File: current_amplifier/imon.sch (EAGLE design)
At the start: 32 parts, among them U1 AD8210, U2 AD1583_AD1583BRTZ-REEL7CT-ND, U3 FR014H5JZ, U4 OP-AMP_BALANCED, U6 LTC2312-12

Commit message: The imon current monitor board schematic is filled out
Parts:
- removed C1, C16: (no value), rcl_custom:C-EU0805-B
- removed R2: (no value), rcl_custom:R-US_0805-B
- removed U1: AD8210, marionette:AD8210
- removed U3: FR014H5JZ, marionette:FR014H5JZ
- added C105, C19: 1u, rcl_custom:C-EU0402-B
- added C18: np, rcl_custom:C-EU0402-B
- added C20: 6.2n, rcl_custom:C-EU0402-B
- added C50: 220p, rcl_custom:C-EU0402-B
- added C80: 100n, rcl_custom:C-EU0402-B
- added D1, D2: ESD8006-ESD8006, marionette:ESD8006-ESD8006
- added J1, R11, R16, R17: (no value), marionette:JUMPER-SHORTED-CUTTABLE-E0402-0.3MM
- added R10: 56, rcl_custom:R-US_0402-B
- added R12, R13, R19: np, rcl_custom:R-US_0402-B
- added R18: 1k, rcl_custom:R-US_0402-B
- added R30: 51, rcl_custom:R-US_0402-B
- added R40: 560, rcl_custom:R-US_0402-B
- added R67, R9: np, rcl_custom:R-US_1206-0402
- added TP1, TP10, TP11, TP9: PAD+VIA_0.25MM, marionette:PAD+VIA_0.25MM
- added TP2: PAD+VIA_0.6MM, marionette:PAD+VIA_0.6MM
- added TP3, TP4, TP5, TP6, TP7, TP8: (no value), marionette:PAD+X-1.0-NO_CREAM+SILK
- added U$1: MCP1501", marionette:MCP1501"
- C10, C3: value (none) -> 100n; device rcl_custom:C-EU0805-B -> rcl_custom:C-EU0402-B
- C11, C12, C13, C14, C15, C4: value (none) -> 1u; device rcl_custom:C-EU0805-B -> rcl_custom:C-EU0402-B
- C2: value (none) -> 2.7n; device rcl_custom:C-EU0805-B -> rcl_custom:C-EU0402-B
- C5: value (none) -> 220p; device rcl_custom:C-EU0805-B -> rcl_custom:C-EU0402-B
- C6, C7: value (none) -> 1u; device rcl_custom:C-EU0805-A-NOSILK -> rcl_custom:C-EU0402-B
- C9: value (none) -> np
- R1: value (none) -> 97.6; device rcl_custom:R-US_0805-B -> rcl_custom:R-US_0402-B
- R3: value (none) -> 88.7; device rcl_custom:R-US_0805-B -> rcl_custom:R-US_0402-B
- R4: value (none) -> 976; device rcl_custom:R-US_0805-B -> rcl_custom:R-US_0402-B
- R5, R6: device rcl_custom:R-US_0805-B -> rcl_custom:R-US_0402-B
- R7, R8: device rcl_custom:R-US_0805-B -> rcl_custom:R-US_1206-0402
- U2: value AD1583_AD1583BRTZ-REEL7CT-ND -> OPAMP_DUALFAN4852; device marionette:VREF_BANDGAP_AD1583_AD1583BRTZ-REEL7CT-ND -> marionette:OPAMP_DUALFAN4852; CHIP ADP1583 -> (none); DPN (none) -> FAN4852IMU8XCT-ND; VREF 3.0V -> (none)
- U4: value OP-AMP_BALANCED -> AD8418; device marionette:OP-AMP_BALANCED -> marionette:AD8418; DPN (none) -> AD8418WBRZ-ND
- U6: DPN (none) -> LTC2312CTS8-12#TRMPBFCT-ND
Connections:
- removed net N$15: R7.1, U1.IN+
- removed net N$7: R6.1, U4G1.BAL2
- new net C80: C6.2, C80.2, U4G3.V-
- new net N$11: R8.1, U4G1.IN-
- new net N$16: R5.2, R6.1, U$1.SHDN_N
- new net N$17: C50.1, R30.1, U2G2.-IN
- new net N$18: C50.2, R16.2, R40.1, TP5.P, U2G2.OUT
- new net N$19: C18.2, R16.1, R17.2, U6.AIN
- new net N$20: D2G3.CATHODE, JP2.1, R11.2
- new net N$21: J1.1, R19.1, TP9.TP, U4G1.VREF2
- new net N$22: R12.1, TP1.TP
- new net VREF_FILTERED: C105.2, C7.2, J1.2, R12.2, R13.1, R18.2, TP10.TP, TP11.TP, U4G1.VREF1
- new net VREF_OUT: R18.1, U$1.VOUT
- net GND: now also C105.1, C14.1, C15.1, C18.1, C19.2, C2.1, C20.1, C7.1, D1G7.PIN, D2G7.PIN, R13.2, R19.2, R5.1, U$1.GND, U2G1.+IN, U2G2.+IN, U2G4.V-; no longer C1.2, C14.2, C15.2, C16.1, C5.2, R3.1, R5.2, R6.2, U1.GND, U1.VREF2, U2.GND, U4G2.VSS
- net N$1: now also R1.2, R11.1, TP3.P, U4G1.VOUT; no longer JP2.1, R1.1, U1.VOUT
- net N$10: now also R67.1, R8.2, R9.1; no longer C6.1, C7.1, R7.2
- net N$12: now also D1G3.CATHODE, TP8.P
- net N$13: now also D1G2.CATHODE, TP7.P
- net N$14: now also D1G1.CATHODE, TP6.P
- net N$2: now also C2.2, R1.1, R3.2, R4.2; no longer C1.1, C2.1, R1.2, R2.1
- net N$3: now also C5.1, R3.1, U2G1.-IN; no longer R2.2, U4G1.+IN
- net N$4: now also C5.2, R10.2, R4.1, TP4.P, U2G1.OUT; no longer R3.2, R4.2, U4G1.-IN
- net N$5: now also D2G1.CATHODE, R17.1; no longer C2.2, R4.1, U4G1.OUT, U6.AIN
- net N$6: now also C20.2, R10.1, R30.2, R40.2; no longer R5.1, U4G1.BAL1
- net N$8: now also R7.1, U4G1.IN+; no longer R8.1, U1.IN-
- net N$9: now also R67.2, R7.2, R9.2; no longer C6.2, C7.2, R8.2
- net V3.3D: now also C19.1, D1G5.CATHODE
- net V5D: now also C14.2, C15.2, C6.1, C80.1, D1G4.CATHODE, R6.2, U$1.VDD, U2G3.V+, U4G2.V+; no longer C14.1, C15.1, C16.2, C5.1, U1.VS, U2.VIN, U4G2.VDD
- net VREF_3.0V: now also TP2.TP; no longer U1.VREF1, U2.VOUT
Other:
- note added: "(2.25V to 5.5V)"
- note added: "(2.5V, 3.3V, 5.0V)"
- note added: "5.5V"
- note added: "Current Monitor Front End"
- note added: "FAN4852"
- note added: "Initial Configuration:"
- note added: "LTC2312 notes:"
- note added: "Low Pass 4th or. Bessel Filter"
- note added: "MCP1501"
- note added: "Maximum 300pF output cap on mic1501. Larger capacitors may be used if there is a resistor in series to make a low pass filter. For example a 1kOhm and a 2.2uF."
- note added: "See ipython notebook documentation: marionette_hardware/current_monitor/design/imon_notes.ipynb for bessel filter values script."
- note added: "Supply Voltage to LTC2312 are (2.7V, 3.6V) and (4.75V, 5.25V). There is a forbidden zone in between that will interfere with operation of the internal voltage reference presumably."
- note added: "The initial configuration of the ADP8418 is for a zero reference point of 2.048 V. The ADP8418 is bidirectional. The gain of the ADP8418 is 20, and the bessel filter of 100 This is for a shunt voltage of 20mV."
- note added: "The internal bandgap reference is scaled by the supply voltage: Vdd = (2.7V, 3.6V) -> Vref = 2.048V Vdd = (4.75V, 5.25V) -> Vref = 4.096V An external reference may be used if the internal reference is overdriven by at least 50mV."
- note added: "Unused TVS diodes"
- note removed: "(3.1V to 2.6V)"
- note removed: "---"
- note removed: "CR2032"
- note removed: "Current Measurement Board"
- note removed: "Front End"
- note removed: "Low Pass Filter Adjustable Gain"
- note removed: "Needs EN or OFF switch on ADC and REF?"
- note removed: "Reference Voltage"
- moved on the sheet: C10, C11, C12, C13, C14, C15, C2, C3, C4, C5, C6, C7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

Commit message: laying out imon.brd
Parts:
- removed D2: ESD8006-ESD8006, marionette:ESD8006-ESD8006
- removed JP3: (no value), pinhead:PINHD-1X7
- removed U$1: MCP1501", marionette:MCP1501"
- added FIDUCIAL1, FIDUCIAL2, FIDUCIAL3, FIDUCIAL4, FIDUCIAL5, FIDUCIAL6: FIDUCIAL-1.0X2.5, marionette:FIDUCIAL-1.0X2.5
- added R14: np, rcl_custom:R-US_0402-B
- added R2: (no value), marionette:JUMPER-SHORTED-CUTTABLE-E0402-0.3MM
- added TP12, TP14: PAD+VIA_0.25MM, marionette:PAD+VIA_0.25MM
- added TP13: PAD+VIA_GND_0.25MM, marionette:PAD+VIA_GND_0.25MM
- added U5: MCP1501", marionette:MCP1501"
- C13: value 1u -> 10u; device rcl_custom:C-EU0402-B -> rcl_custom:C-EU0805-B
- C8, R5: value (none) -> np
- JP2: device pinhead:PINHD-1X4 -> pinhead:PINHD-2X12/90
- R6: value (none) -> 10k
- TP11: value PAD+VIA_0.25MM -> PAD+VIA_0.6MM; device marionette:PAD+VIA_0.25MM -> marionette:PAD+VIA_0.6MM
- TP3: value (none) -> PAD+VIA_GND_0.25MM; device marionette:PAD+X-1.0-NO_CREAM+SILK -> marionette:PAD+VIA_GND_0.25MM
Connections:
- net N$10 renamed VSHUNT_M
- net N$11 renamed VSHUNT_FILTERED_M
- net N$17 renamed FILTER2-
- net N$18 renamed FILTER_2_OUT
- net N$2 renamed FILTER_1_V1
- net N$21 renamed AD8418_REF2
- net N$22 renamed VREF_OPTIONAL
- net N$3 renamed FILTER1-
- net N$4 renamed FILTER_1_OUT
- net N$6 renamed FILTER_2_V1
- net N$8 renamed VSHUNT_FILTERED_P
- net N$9 renamed VSHUNT_P
- net VREF_3.0V renamed ADC_VREF
- removed net C80: C6.2, C80.2, U4G3.V-
- removed net N$1: R1.2, R11.1, TP3.P, U4G1.VOUT
- removed net N$12: D1G3.CATHODE, JP3.5, TP8.P, U6.SDO
- removed net N$13: D1G2.CATHODE, JP3.6, TP7.P, U6.SCK
- removed net N$14: D1G1.CATHODE, JP3.7, TP6.P, U6.CONV
- removed net N$16: R5.2, R6.1, U$1.SHDN_N
- removed net N$19: C18.2, R16.1, R17.2, U6.AIN
- removed net N$20: D2G3.CATHODE, JP2.1, R11.2
- removed net N$5: D2G1.CATHODE, JP2.3, R17.1
- new net ADC_AIN: R2.1, U6.AIN
- new net ADC_CONV: D1G1.CATHODE, JP2.21, JP2.22, TP6.P, U6.CONV
- new net ADC_SCK: D1G2.CATHODE, JP2.19, JP2.20, TP7.P, U6.SCK
- new net ADC_SDO: D1G3.CATHODE, JP2.17, JP2.18, TP8.P, U6.SDO
- new net MCP1501_SHDN_N: R5.2, R6.1, U5.SHDN_N
- new net VSHUNT_20X: R1.2, R11.1, TP12.TP, U4G1.VOUT
- new net VSHUNT_20X_OUT: D1G6.CATHODE, JP2.3, JP2.4, R11.2
- new net VSHUNT_FILTERED: D1G4.CATHODE, JP2.5, JP2.6, R17.1
- new net VSHUNT_FILTERED_ADC: C18.2, R14.1, R16.1, R17.2, R2.2, TP14.TP
- net GND: now also C6.2, C80.2, JP2.1, JP2.11, JP2.12, JP2.15, JP2.16, JP2.23, JP2.24, JP2.7, JP2.8, R14.2, TP13.TP, TP3.TP, U4G3.V-, U5.GND; no longer D2G7.PIN, JP2.4, JP3.2, JP3.4, U$1.GND
- net V3.3D: now also JP2.13, JP2.14; no longer JP3.3
- net V5D: now also JP2.10, JP2.9, U5.VDD; no longer D1G4.CATHODE, JP3.1, U$1.VDD
- net VREF_OUT: now also U5.VOUT; no longer U$1.VOUT
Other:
- note added: "R16 and R14 can voltage divide the bessel filter output."
- note removed: "Unused TVS diodes"
- moved on the sheet: C105, C14, C15, C3, C4, C7, J1, R12, R13, R18, R19, R5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

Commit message: current monitor layout in progress
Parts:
- added C1: 10n, rcl_custom:C-EU0402-B
- added J2, J3: (no value), marionette:JUMPER-SHORTED-CUTTABLE-E0603-0.8MM
- added JP4: (no value), pinhead:PINHD-2X6/90
- added R15: (no value), marionette:JUMPER-SHORTED-CUTTABLE-E0402-0.3MM
- JP1: device pinhead:PINHD-1X2 -> pinhead:PINHD-2X2
- JP2: device pinhead:PINHD-2X12/90 -> pinhead:PINHD-2X4
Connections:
- new net ADC_VREF_CUTTABLE: R15.1, U6.REF
- new net V3.3D_CUTTABLE: J3.1, U6.DVDD
- new net V5D_CUTTABLE: J2.1, U6.VDD
- net ADC_CONV: now also JP4.10, JP4.9; no longer JP2.21, JP2.22
- net ADC_SCK: now also JP4.7, JP4.8; no longer JP2.19, JP2.20
- net ADC_SDO: now also JP4.5, JP4.6; no longer JP2.17, JP2.18
- net ADC_VREF: now also R15.2; no longer U6.REF
- net GND: now also C1.1, JP4.11, JP4.12; no longer JP2.1, JP2.11, JP2.12, JP2.15, JP2.16, JP2.2, JP2.23, JP2.24
- net V3.3D: now also J3.2, JP4.3, JP4.4; no longer JP2.13, JP2.14, U6.DVDD
- net V5D: now also D1G6.CATHODE, J2.2, JP4.1, JP4.2; no longer JP2.10, JP2.9, U6.VDD
- net VREF_FILTERED: now also C1.2, JP2.5, JP2.6
- net VSHUNT_20X_OUT: now also JP2.1, JP2.2; no longer D1G6.CATHODE, JP2.3, JP2.4
- net VSHUNT_FILTERED: now also JP2.3, JP2.4; no longer D1G4.CATHODE, JP2.5, JP2.6
- net VSHUNT_M: now also JP1.3, JP1.4; no longer JP1.1
- net VSHUNT_P: now also JP1.1
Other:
- moved on the sheet: C105, C14, C15, C7, R18, R2, R5, R6, TP2, U5

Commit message: The current monitor board is laid out but needs some polishing
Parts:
- removed TP10: PAD+VIA_0.25MM, marionette:PAD+VIA_0.25MM
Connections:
- net ADC_CONV: now also D1G3.CATHODE, JP4.5, JP4.6; no longer D1G1.CATHODE, JP4.10, JP4.9
- net ADC_SDO: now also D1G1.CATHODE, JP4.10, JP4.9; no longer D1G3.CATHODE, JP4.5, JP4.6
- net VREF_FILTERED: no longer TP10.TP
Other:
- moved on the sheet: C10, C11, C12, C13, C18, C19, C2, C20, C3, C4, C5, C50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

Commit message: imon board passes 6mil DRC.  The gain on the 4th order Bessel filter is probably wrong and needs to be redone, but the layout is ready for review
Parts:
- removed R13, R14: np, rcl_custom:R-US_0402-B
- removed R67, R9: np, rcl_custom:R-US_1206-0402
- removed TP11: PAD+VIA_0.6MM, marionette:PAD+VIA_0.6MM
- removed TP12: PAD+VIA_0.25MM, marionette:PAD+VIA_0.25MM
- removed TP3: PAD+VIA_GND_0.25MM, marionette:PAD+VIA_GND_0.25MM
- removed TP6, TP7, TP8: (no value), marionette:PAD+X-1.0-NO_CREAM+SILK
- added C16: np, rcl_custom:C-EU0402-B
- added C67: np, rcl_custom:C-EU1206-0402
- added H1, H2, H3, H4: M2-BARE_MOUNTING_HOLE, marionette:M2-BARE_MOUNTING_HOLE
- JP2: device pinhead:PINHD-2X4 -> pinhead:PINHD-2X3
- U5: PPM (none) -> 50/degree C
- renumbered J2 to J35, J3 to J36, R11 to J34, R15 to J30, R16 to J32, R17 to J33, R2 to J31
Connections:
- net V3.3D renamed VIO
- net V5D renamed VDD
- net ADC_CONV: no longer TP6.P
- net ADC_SCK: no longer TP7.P
- net ADC_SDO: no longer TP8.P
- net ADC_VREF: now also C16.2
- net GND: now also C16.1, JP2.2, JP2.4, JP2.6; no longer JP2.7, JP2.8, R13.2, R14.2, TP3.TP
- net VREF_FILTERED: now also JP2.1; no longer JP2.5, JP2.6, R13.1, TP11.TP
- net VSHUNT_20X: no longer TP12.TP
- net VSHUNT_20X_OUT: now also JP2.3; no longer JP2.1, JP2.2
- net VSHUNT_FILTERED: now also JP2.5; no longer JP2.3, JP2.4
- net VSHUNT_FILTERED_ADC: no longer R14.1
- net VSHUNT_FILTERED_M: now also C67.1, C8.2
- net VSHUNT_FILTERED_P: now also C67.2, C9.2
- net VSHUNT_M: no longer C8.2, R67.1, R9.1
- net VSHUNT_P: no longer C9.2, R67.2, R9.2
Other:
- note added: "AD8418 common mode input voltage range: (-2V, 70V)"
- note added: "Analog"
- note added: "Bandwidth Notes:"
- note added: "J32 and C18 form the fifth stage of the Bessel filter"
- note added: "Power/Data"
- note added: "The AD8418 has a 3dB BW of 200kHz and a GBW of 1.5MHz. The LTC2312 has 500ksps BW."
- note added: "The initial configuration of the ADP8418 is for a zero reference point of 2.048 V. The ADP8418 is bipolar. The gain of the ADP8418 is 20, and the Bessel filter of 100 This is for a shunt voltage of 20mV."
- note added: "Voltage Reference"
- note removed: "R16 and R14 can voltage divide the bessel filter output."
- note removed: "The initial configuration of the ADP8418 is for a zero reference point of 2.048 V. The ADP8418 is bidirectional. The gain of the ADP8418 is 20, and the bessel filter of 100 This is for a shunt voltage of 20mV."
- moved on the sheet: C1, C105, C14, C15, C7, C8, C9, J1, JP4, R12, R18, R19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

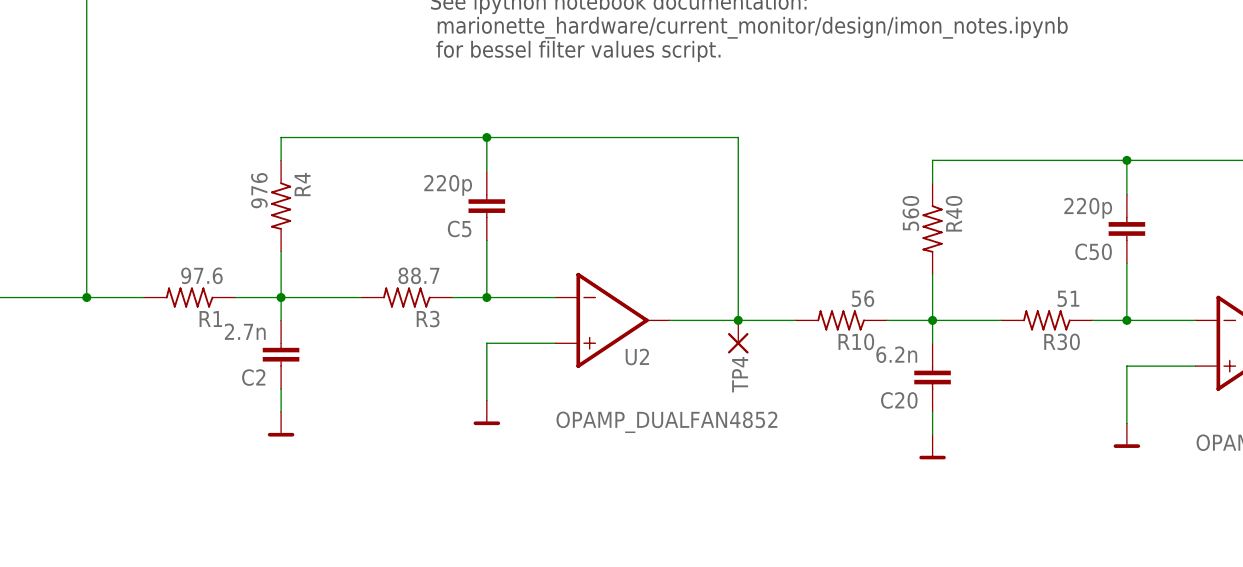
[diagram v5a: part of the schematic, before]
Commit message: Changed the gain on the Bessel filter
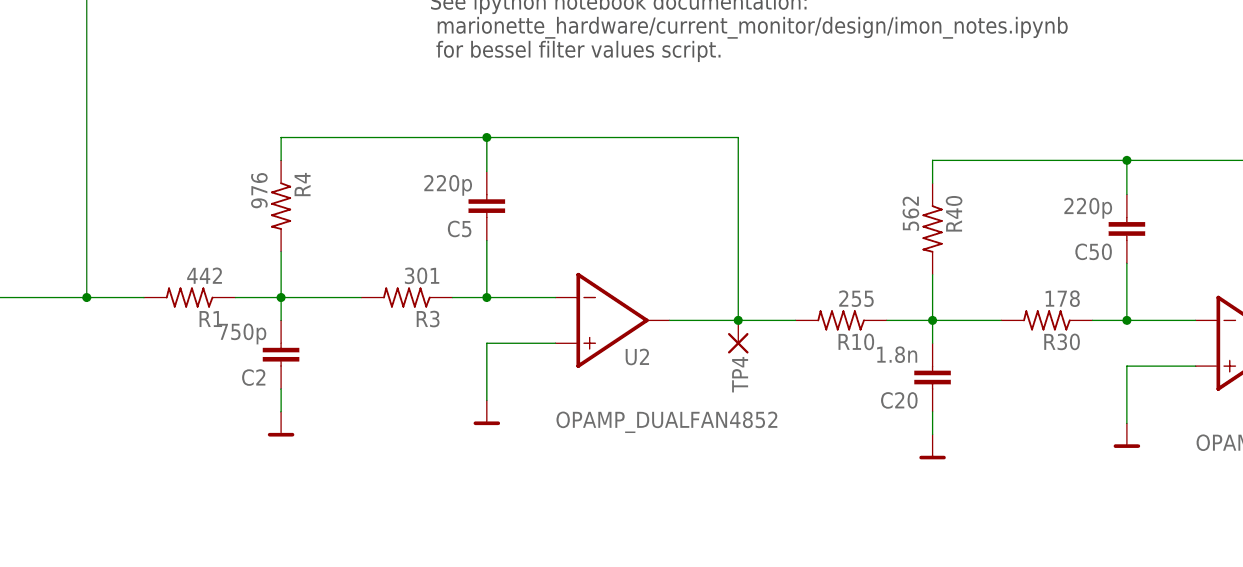
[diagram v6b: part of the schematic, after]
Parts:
- C2: value 2.7n -> 750p
- C20: value 6.2n -> 1.8n
- R1: value 97.6 -> 442
- R10: value 56 -> 255
- R3: value 88.7 -> 301
- R30: value 51 -> 178
- R40: value 560 -> 562
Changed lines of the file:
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@@
 <setting verticaltext="up"/>
 </settings>
-<grid distance="0.05" unitdist="inch" unit="inch" style="lines" multiple="2" display="no" altdistance="0.01" altunitdist="inch" altunit="inch"/>
+<grid distance="0.1" unitdist="inch" unit="inch" style="lines" multiple="1" display="no" altdistance="0.01" altunitdist="inch" altunit="inch"/>
 <layers>
 <layer number="1" name="Top" color="4" fill="1" visible="no" active="no"/>
@@
 <part name="C3" library="rcl_custom" deviceset="C-EU" device="0402-B" value="100n"/>
 <part name="C4" library="rcl_custom" deviceset="C-EU" device="0402-B" value="1u"/>
-<part name="R3" library="rcl_custom" deviceset="R-US_" device="0402-B" value="88.7"/>
-<part name="R1" library="rcl_custom" deviceset="R-US_" device="0402-B" value="97.6"/>
+<part name="R3" library="rcl_custom" deviceset="R-US_" device="0402-B" value="301"/>
+<part name="R1" library="rcl_custom" deviceset="R-US_" device="0402-B" value="442"/>
 <part name="C5" library="rcl_custom" deviceset="C-EU" device="0402-B" value="220p"/>
-<part name="C2" library="rcl_custom" deviceset="C-EU" device="0402-B" value="2.7n"/>
+<part name="C2" library="rcl_custom" deviceset="C-EU" device="0402-B" value="750p"/>
 <part name="C80" library="rcl_custom" deviceset="C-EU" device="0402-B" value="100n"/>
 <part name="C6" library="rcl_custom" deviceset="C-EU" device="0402-B" value="1u"/>
@@
 <part name="GND12" library="supply" deviceset="GND" device=""/>
 <part name="GND18" library="supply" deviceset="GND" device=""/>
-<part name="R30" library="rcl_custom" deviceset="R-US_" device="0402-B" value="51"/>
-<part name="R10" library="rcl_custom" deviceset="R-US_" device="0402-B" value="56"/>
+<part name="R30" library="rcl_custom" deviceset="R-US_" device="0402-B" value="178"/>
+<part name="R10" library="rcl_custom" deviceset="R-US_" device="0402-B" value="255"/>
 <part name="C50" library="rcl_custom" deviceset="C-EU" device="0402-B" value="220p"/>
-<part name="C20" library="rcl_custom" deviceset="C-EU" device="0402-B" value="6.2n"/>
-<part name="R40" library="rcl_custom" deviceset="R-US_" device="0402-B" value="560"/>
+<part name="C20" library="rcl_custom" deviceset="C-EU" device="0402-B" value="1.8n"/>
+<part name="R40" library="rcl_custom" deviceset="R-US_" device="0402-B" value="562"/>
 <part name="J32" library="marionette" deviceset="JUMPER-SHORTED-CUTTABLE" device="-E0402-0.3MM"/>
 <part name="C18" library="rcl_custom" deviceset="C-EU" device="0402-B" value="np"/>

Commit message: Gerber files and small layout changes to the imon.brd
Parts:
- added R2: 10k, rcl_custom:R-US_0402-B
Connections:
- net ADC_CONV: now also R2.2
- net VIO: now also R2.1
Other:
- note added: "The IN+ has significantly more input bias current (150uA, 250uA) while the IN- has < 50uA bias current."
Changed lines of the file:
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@@
 <part name="H3" library="marionette" deviceset="M2-BARE_MOUNTING_HOLE" device=""/>
 <part name="H4" library="marionette" deviceset="M2-BARE_MOUNTING_HOLE" device=""/>
+<part name="R2" library="rcl_custom" deviceset="R-US_" device="0402-B" value="10k"/>
 </parts>
 <sheets>
@@
 <text x="218.44" y="182.88" size="5.08" layer="97">Voltage Reference</text>
 <text x="17.78" y="193.04" size="1.778" layer="97">AD8418 common mode input voltage range: (-2V, 70V)</text>
+<text x="17.78" y="185.42" size="1.778" layer="97">The IN+ has significantly more input bias current (150uA, 250uA)
+while the IN- has &lt; 50uA bias current.</text>
 </plain>
 <instances>
@@
 <instance part="H3" gate="G$1" x="80.01" y="15.24"/>
 <instance part="H4" gate="G$1" x="99.06" y="15.24"/>
+<instance part="R2" gate="R" x="474.98" y="215.9" rot="R270"/>
 </instances>
 <busses>
@@
 <wire x1="449.58" y1="203.2" x2="467.36" y2="203.2" width="0.1524" layer="91"/>
 <pinref part="D1" gate="G3" pin="CATHODE"/>
-<wire x1="467.36" y1="203.2" x2="486.41" y2="203.2" width="0.1524" layer="91"/>
+<wire x1="467.36" y1="203.2" x2="474.98" y2="203.2" width="0.1524" layer="91"/>
 <junction x="467.36" y="203.2"/>
+<wire x1="474.98" y1="203.2" x2="486.41" y2="203.2" width="0.1524" layer="91"/>
 <wire x1="486.41" y1="203.2" x2="494.03" y2="208.28" width="0.1524" layer="91"/>
 <wire x1="494.03" y1="208.28" x2="519.43" y2="208.28" width="0.1524" layer="91"/>
@@
 <junction x="519.43" y="208.28"/>
 <label x="497.84" y="208.28" size="1.778" layer="95"/>
+<pinref part="R2" gate="R" pin="2"/>
+<wire x1="474.98" y1="210.82" x2="474.98" y2="203.2" width="0.1524" layer="91"/>
+<junction x="474.98" y="203.2"/>
 </segment>
 </net>
@@
 <junction x="527.05" y="210.82"/>
 <wire x1="519.43" y1="210.82" x2="483.87" y2="210.82" width="0.1524" layer="91"/>
-<wire x1="483.87" y1="210.82" x2="483.87" y2="261.62" width="0.1524" layer="91"/>
+<wire x1="483.87" y1="210.82" x2="483.87" y2="223.52" width="0.1524" layer="91"/>
 <junction x="519.43" y="210.82"/>
+<wire x1="483.87" y1="223.52" x2="483.87" y2="261.62" width="0.1524" layer="91"/>
 <wire x1="483.87" y1="261.62" x2="436.88" y2="261.62" width="0.1524" layer="91"/>
 <pinref part="C12" gate="CE" pin="1"/>
@@
 <label x="497.84" y="210.82" size="1.778" layer="95"/>
 <pinref part="V1" gate="G1" pin="VIO"/>
-</segment>
-</net>
+<pinref part="R2" gate="R" pin="1"/>
+<wire x1="474.98" y1="220.98" x2="474.98" y2="223.52" width="0.1524" layer="91"/>
+<wire x1="474.98" y1="223.52" x2="483.87" y2="223.52" width="0.1524" layer="91"/>
+<junction x="483.87" y="223.52"/>
+</segment>
+</net>
